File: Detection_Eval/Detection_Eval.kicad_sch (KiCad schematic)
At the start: 1 part, among them U1 ESP8266

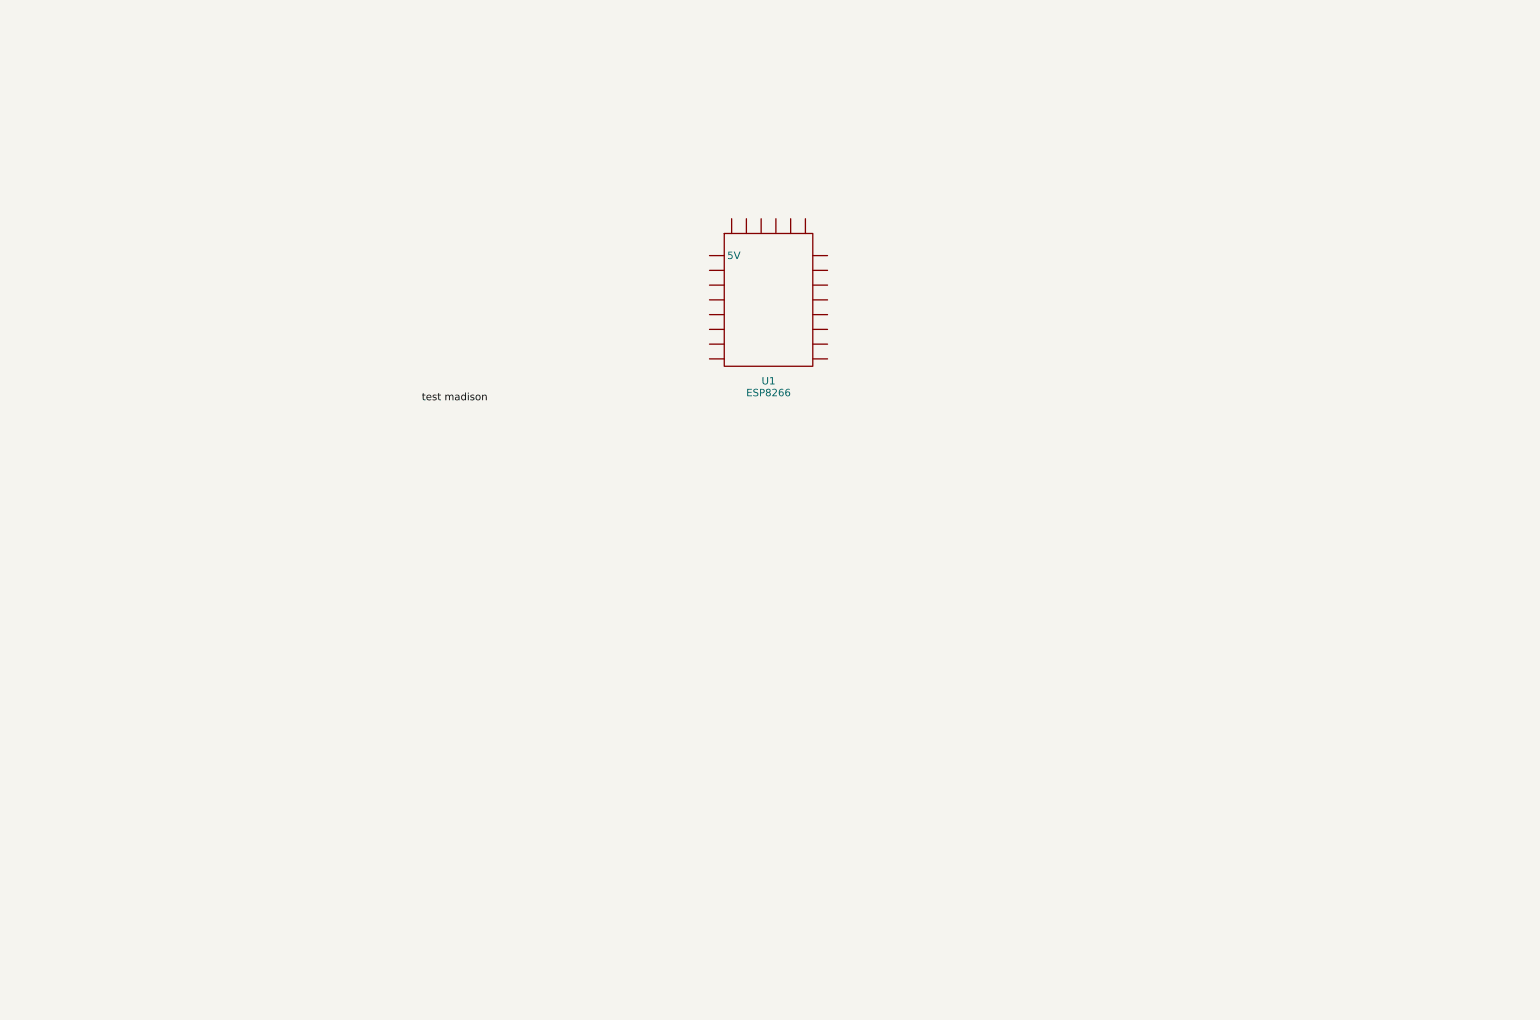
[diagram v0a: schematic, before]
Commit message: Madison_01-16
Updated ESP, MP3 symbols
Added speaker and USB connection
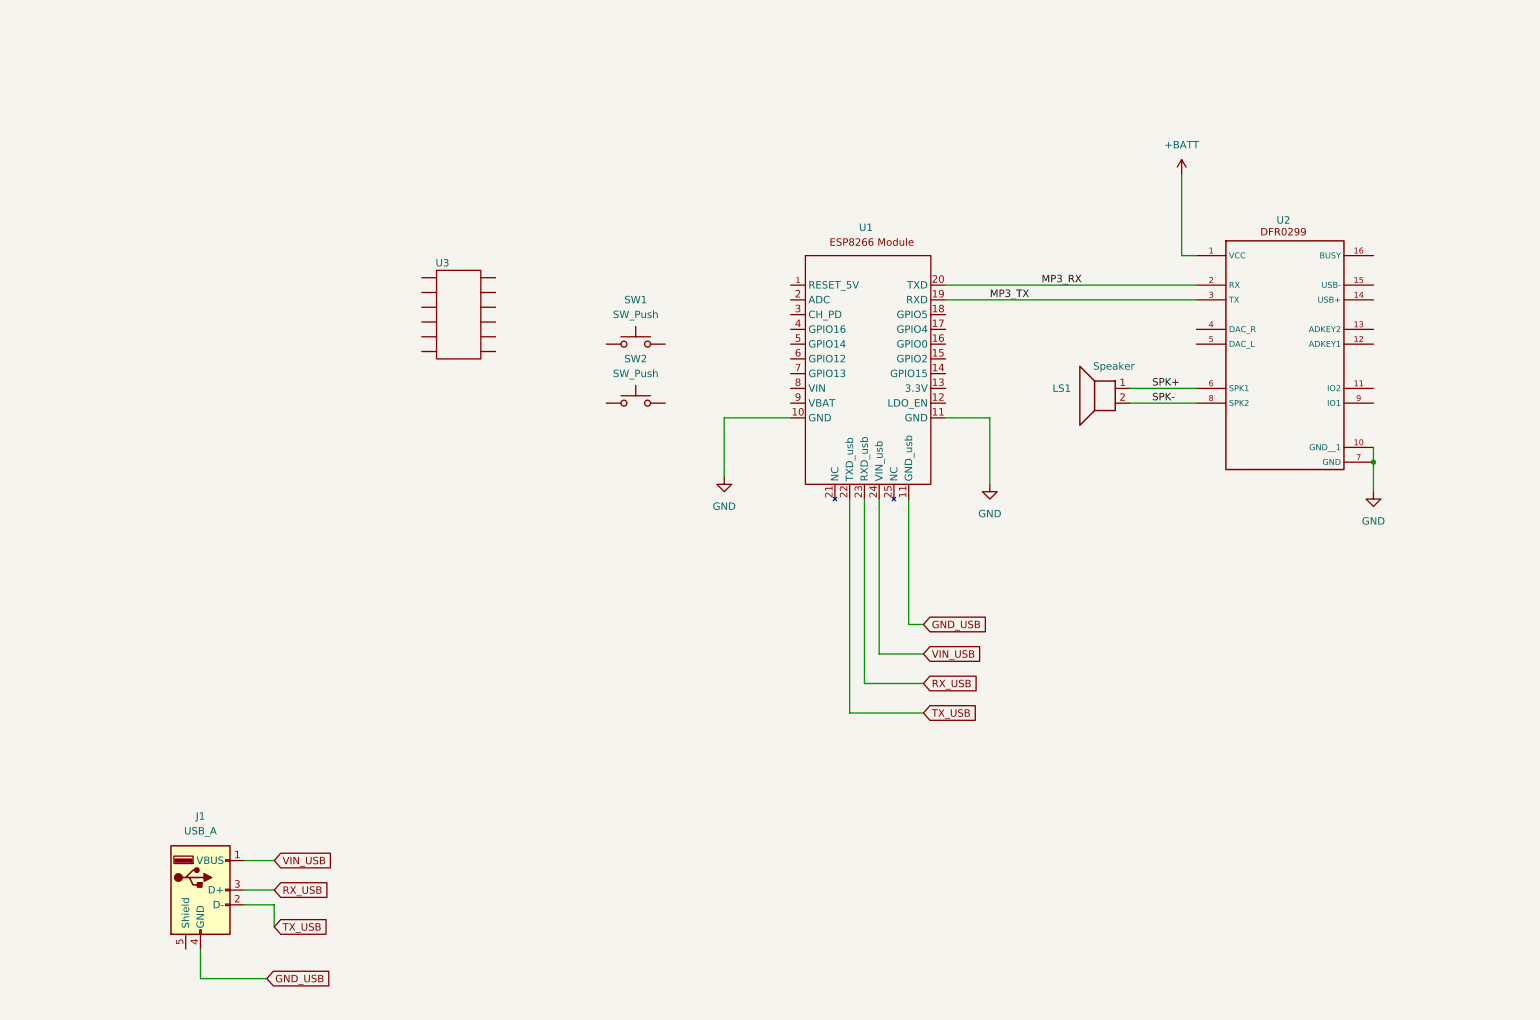
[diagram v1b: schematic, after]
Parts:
- added J1: USB_A, symbol Connector:USB_A
- added LS1: Speaker, symbol Device:Speaker
- added SW1, SW2: SW_Push, symbol Switch:SW_Push
- added U2: ~, symbol Detection_Eval_lib:DFR0299
- added U3: ~, symbol Detection_Eval_lib:Accelerometer
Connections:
- new net +BATT: U2.1 (VCC)
- new net GND: U1.10 (GND), U1.11 (GND_usb), U2.10 (GND__1), U2.7 (GND)
- new net GND_USB: J1.4 (GND), U1.11 (GND_usb)
- new net MP3_RX: U1.20 (TXD), U2.2 (RX)
- new net MP3_TX: U1.19 (RXD), U2.3 (TX)
- new net RX_USB: J1.3 (D+), U1.23 (RXD_usb)
- new net SPK+: LS1.1, U2.6 (SPK1)
- new net SPK-: LS1.2, U2.8 (SPK2)
- new net TX_USB: J1.2 (D-), U1.22 (TXD_usb)
- new net VIN_USB: J1.1 (VBUS), U1.24 (VIN_usb)

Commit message: Madison_01-16pt2
Added LED, Button and accelerometer circuit
Updated accelerometer symbol
Updated title block
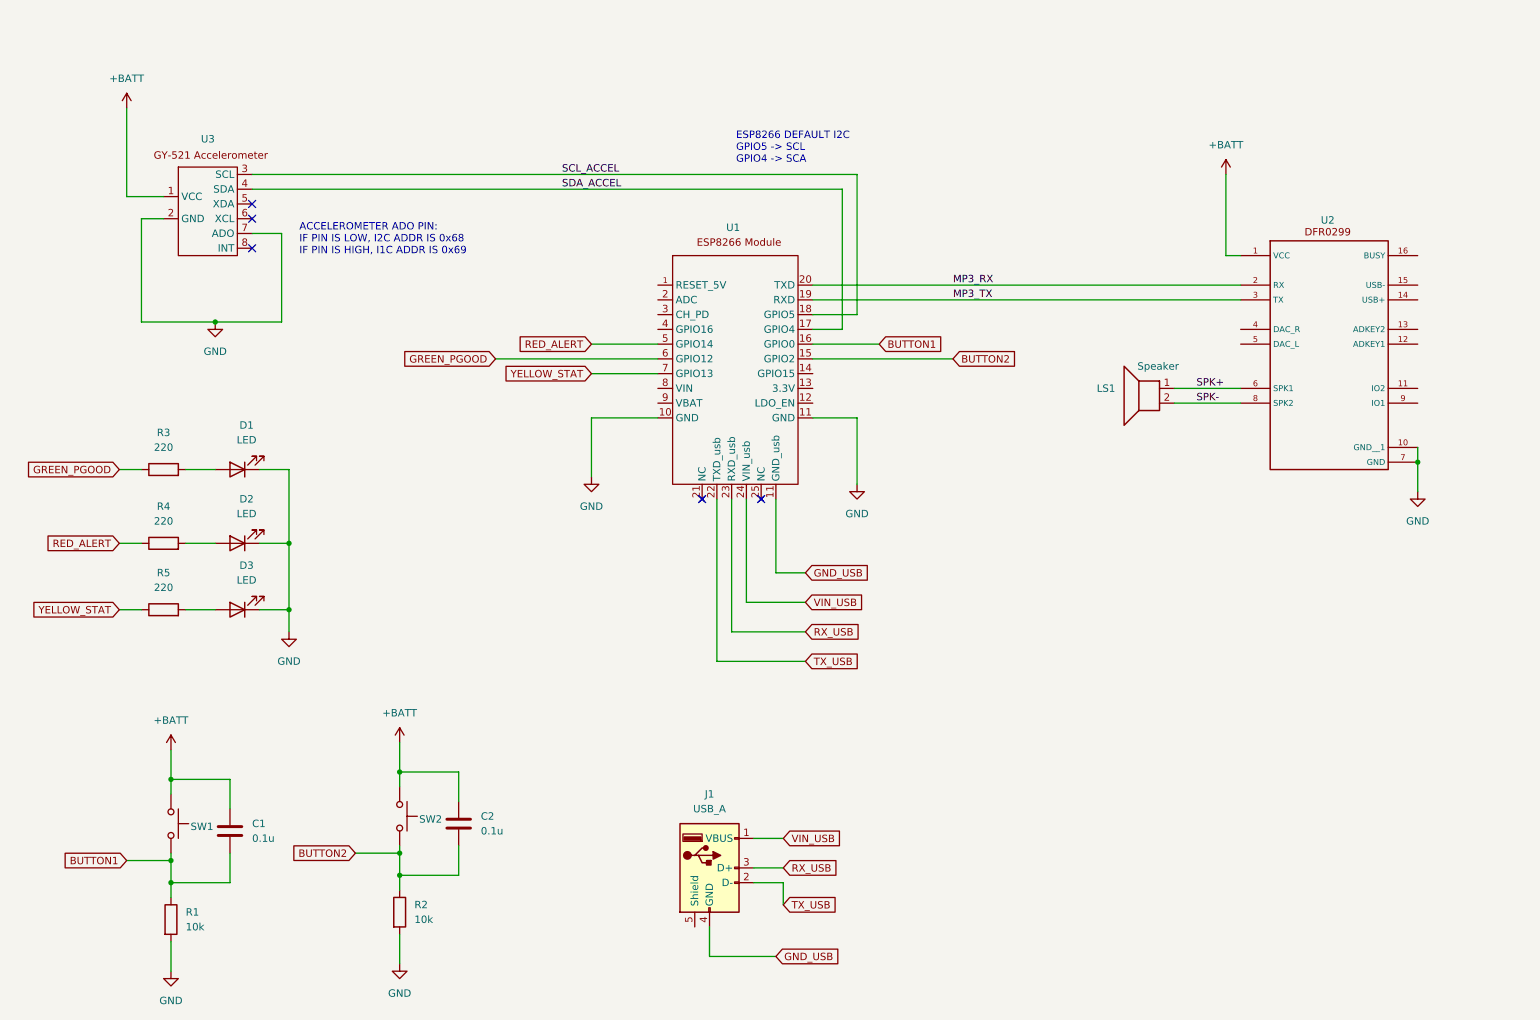
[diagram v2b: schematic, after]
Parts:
- added C1, C2: 0.1u, symbol Device:C
- added D1, D2, D3: LED, symbol Device:LED
- added R1, R2: 10k, symbol Device:R
- added R3, R4, R5: 220, symbol Device:R
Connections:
- net +BATT: now also SW1.1, SW2.1, U3.1 (VCC), C1.1, C2.1
- net GND: now also U3.2 (GND), U3.7 (ADO), D1.1 (K), D2.1 (K), D3.1 (K), R1.2, R2.2
- net BUTTON1: now reaches SW1.2
- net BUTTON1: now also U1.16 (GPIO0), C1.2, R1.1
- net BUTTON2: now reaches U1.15 (GPIO2)
- net BUTTON2: now also SW2.2, C2.2, R2.1
- net SDA_ACCEL: now reaches U1.17 (GPIO4)
- net SDA_ACCEL: now also U3.4 (SDA)
- net SCL_ACCEL: now reaches U1.18 (GPIO5)
- net SCL_ACCEL: now also U3.3 (SCL)
- net RED_ALERT: now reaches U1.5 (GPIO14)
- net RED_ALERT: now also R4.1
- net GREEN_PGOOD: now reaches U1.6 (GPIO12)
- net GREEN_PGOOD: now also R3.1
- net YELLOW_STAT: now reaches U1.7 (GPIO13)
- net YELLOW_STAT: now also R5.1
- new net: D2.2 (A), R4.2
- new net: D3.2 (A), R5.2
- new net: D1.2 (A), R3.2
- no-connect marks 0 -> 5
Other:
- note added: "ACCELEROMETER ADO PIN: IF PIN IS LOW, I2C ADDR IS 0x68 IF PIN IS HIGH, I1C ADDR IS 0x69"
- note added: "ESP8266 DEFAULT I2C GPIO5 -> SCL GPIO4 -> SCA"
- company: (none) -> Capstone G12 - Auto-Injection Mechanism for Seizure Medication
- title: (none) -> Detection Module
- moved on the sheet: J1, LS1, SW1, U1, U2

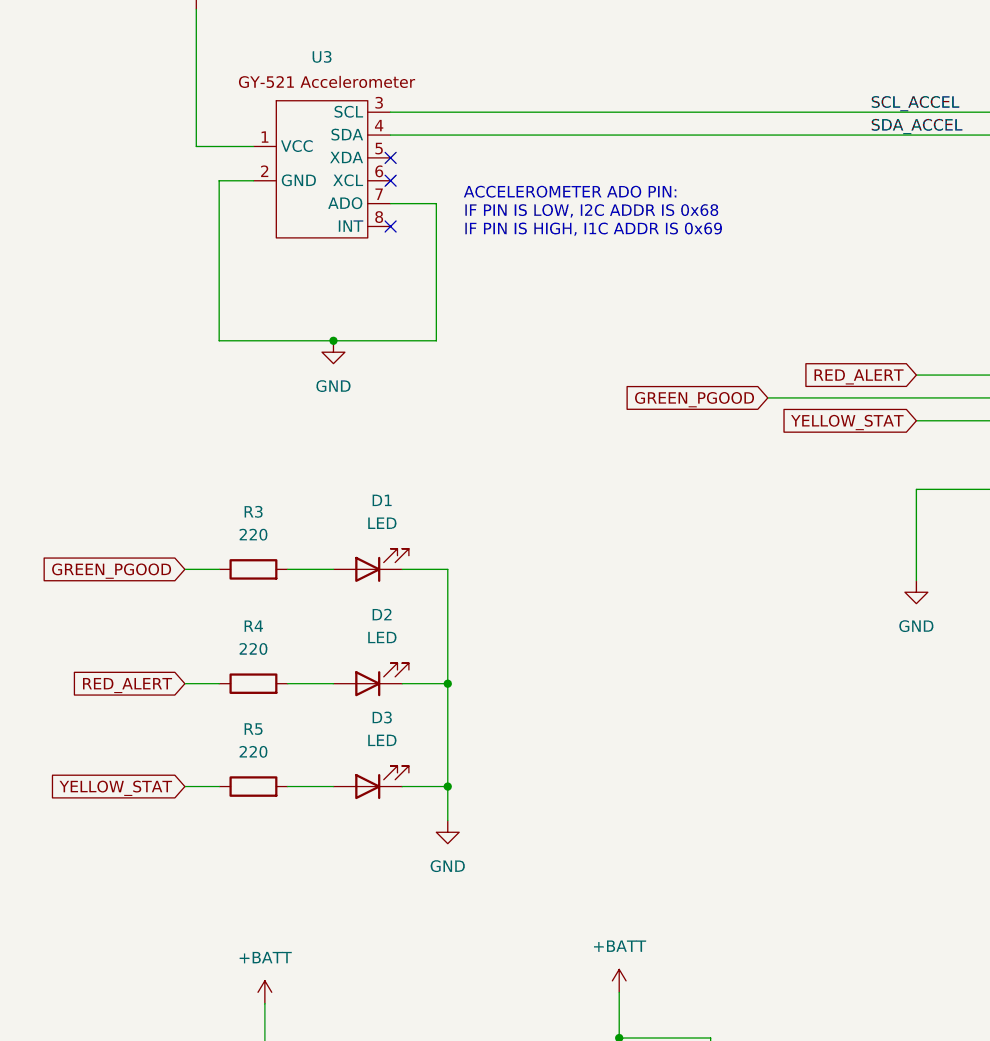
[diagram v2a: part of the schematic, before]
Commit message: Madison_01-20
Adding footprints 1
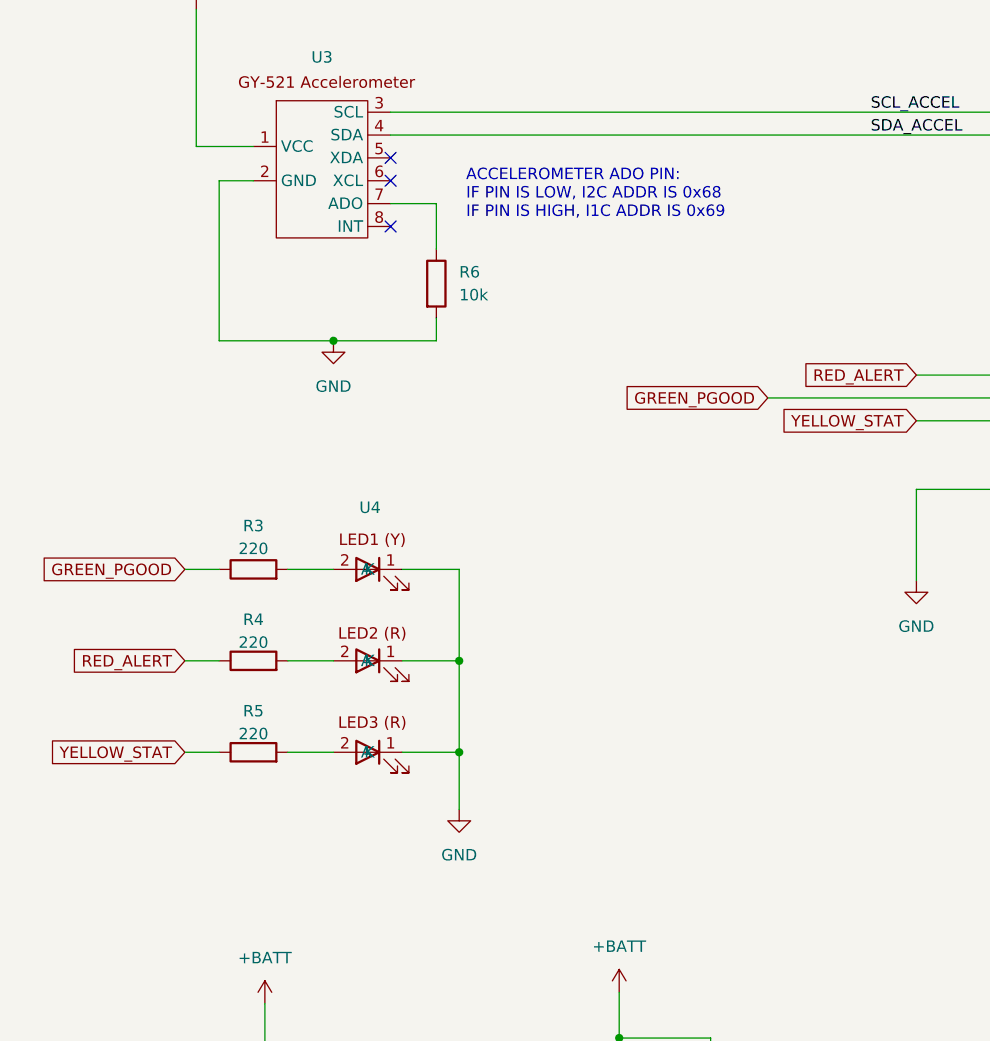
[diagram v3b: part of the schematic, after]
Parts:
- removed D1, D2, D3: LED, symbol Device:LED
- added R6: 10k, Resistor_SMD:R_0402_1005Metric, symbol Device:R
- added U4: ~, symbol Detection_Eval_lib:DIALIGHT_3LED
- R1, R2, R3, R4, R5: footprint (none) -> Resistor_SMD:R_0402_1005Metric
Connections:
- net GND: now also R6.2, U4.1 (K); no longer U3.7 (ADO)
- net at R4.2: now also U4.2 (A)
- net at R5.2: now also U4.2 (A)
- net at R3.2: now also U4.2 (A)
- new net: R6.1, U3.7 (ADO)
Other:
- moved on the sheet: R4, R5

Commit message: Madison_01-20_2
Updated further footprints
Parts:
- U4: footprint (none) -> Detection_Eval_lib_fp:DIALIGHT_3LED
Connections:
- net GND: now also U4.3 (K), U4.5 (K)
- net at U4.2 (A): now also R3.2; no longer R4.2
- net at R5.2: now also U4.6 (A); no longer U4.2 (A)
- new net: R4.2, U4.4 (A)
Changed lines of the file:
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@@
 			)
 		)
-		(property "Footprint" ""
+		(property "Footprint" "Detection_Eval_lib_fp:DIALIGHT_3LED"
 			(at 50.8 120.65 0)
 			(effects
@@
 			)
 		)
-		(pin "1"
+		(pin "6"
 		)
 		(pin "2"
 		)
-		(pin "2"
+		(pin "3"
 		)
-		(pin "2"
+		(pin "5"
+		)
+		(pin "4"
 		)
 		(pin "1"
-		)
-		(pin "1"

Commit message: Madison_01-21
Further sch updates based on review
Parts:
- added R10, R7, R8, R9: 0, Resistor_SMD:R_0402_1005Metric, symbol Device:R
- R3, R4, R5: value 220 -> 150
- R6: value 10k -> 0
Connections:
- net +BATT: now also R10.1, R7.1
- net BUTTON1: now also U1.6 (GPIO12); no longer U1.16 (GPIO0)
- net BUTTON2: now also U1.7 (GPIO13); no longer U1.15 (GPIO2)
- net GND: now also U3.7 (ADO); no longer R6.2
- net LED1: now reaches R6.1
- net LED1: now also U1.16 (GPIO0); no longer U3.7 (ADO)
- net LED3: now reaches U1.14 (GPIO15)
- net LED3: now also R9.1
- net at U1.8 (VIN): now also R7.2
- net at U1.9 (VBAT): now also R10.2
- net GREEN_PGOOD: no longer names the net of R3.1
- net GREEN_PGOOD: now also R6.2; no longer U1.6 (GPIO12)
- net RED_ALERT: no longer names the net of R4.1
- net RED_ALERT: now also R8.2; no longer U1.5 (GPIO14)
- net YELLOW_STAT: no longer names the net of R5.1
- net YELLOW_STAT: now also R9.2; no longer U1.7 (GPIO13)
- new net LED2: R8.1, U1.15 (GPIO2)
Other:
- note added: "DO NOT POPULATE PLACEHOLDER FOR NOW"
- moved on the sheet: U3

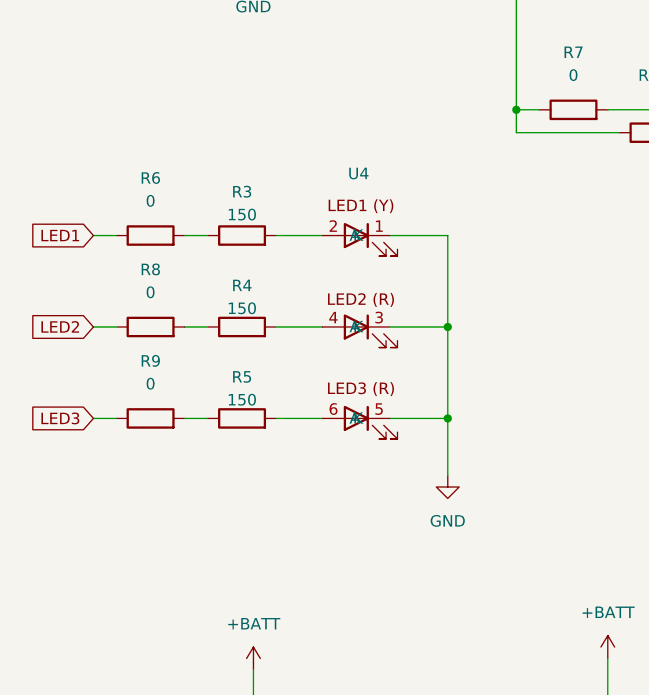
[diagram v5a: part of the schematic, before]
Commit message: Update Detection_Eval.kicad_sch
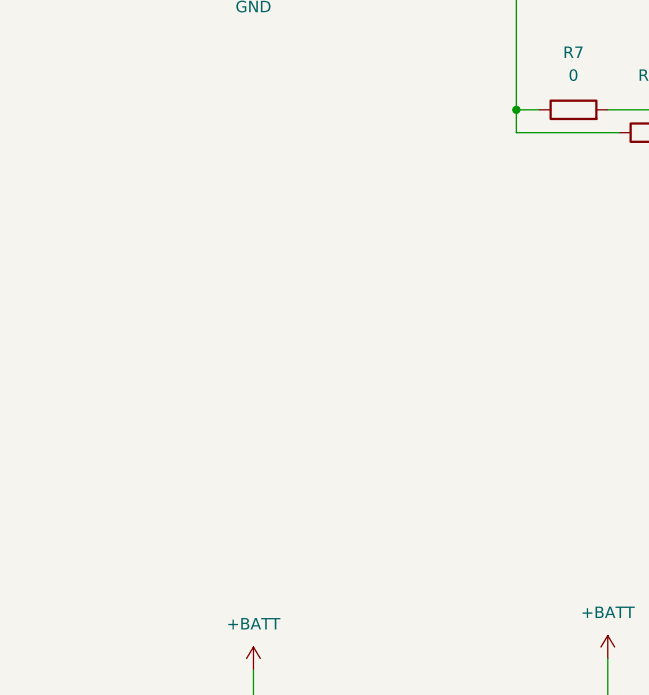
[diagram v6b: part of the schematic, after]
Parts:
- removed R3, R4, R5: 150, Resistor_SMD:R_0402_1005Metric, symbol Device:R
- removed R6, R8, R9: 0, Resistor_SMD:R_0402_1005Metric, symbol Device:R
- removed U4: ~, Detection_Eval_lib_fp:DIALIGHT_3LED, symbol Detection_Eval_lib:DIALIGHT_3LED
